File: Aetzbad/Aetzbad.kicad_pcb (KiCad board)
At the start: 2 copper layers, 13 parts, among them J1 CONN_01X04_MALE, J2 CONN_01X04_MALE, J3 CONN_01X04_MALE, J4 CONN_01X03_MALE, J5 CONN_01X03, Q1 BC547

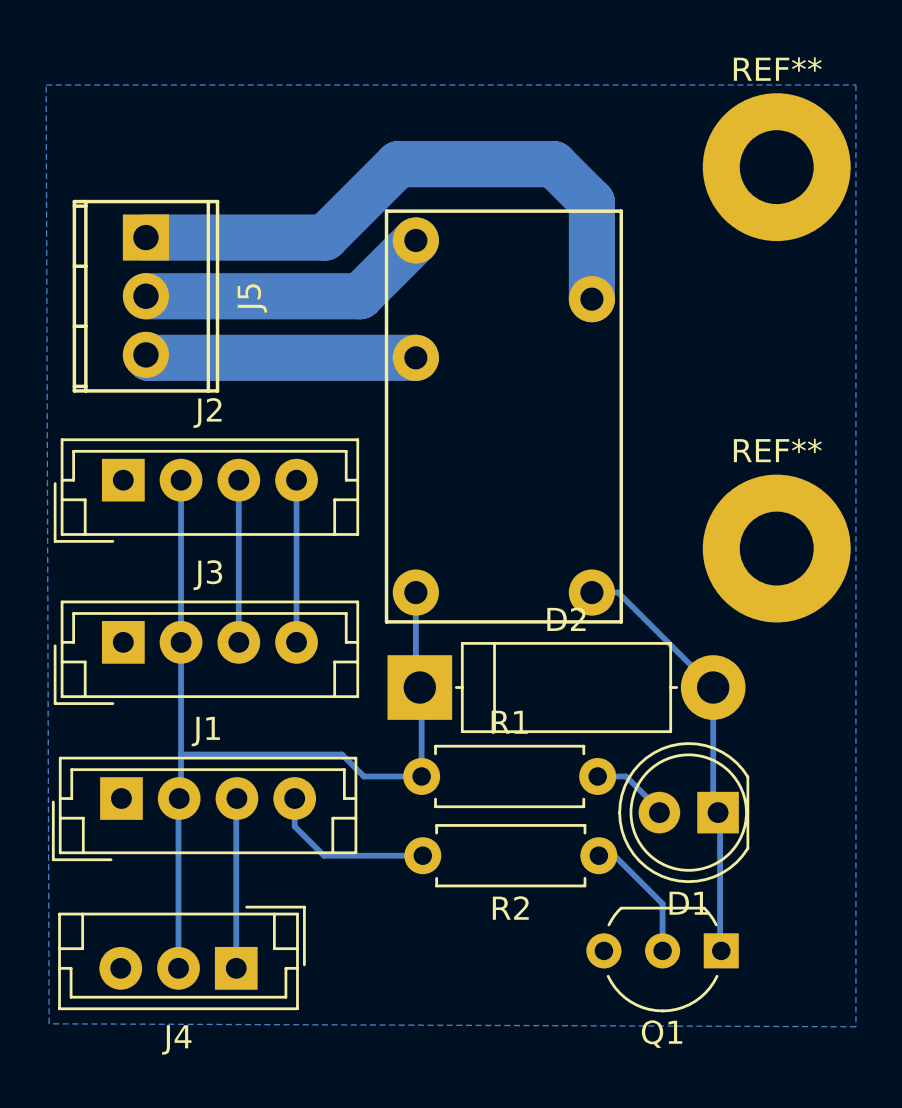
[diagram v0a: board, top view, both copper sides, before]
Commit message: added 3d Relais
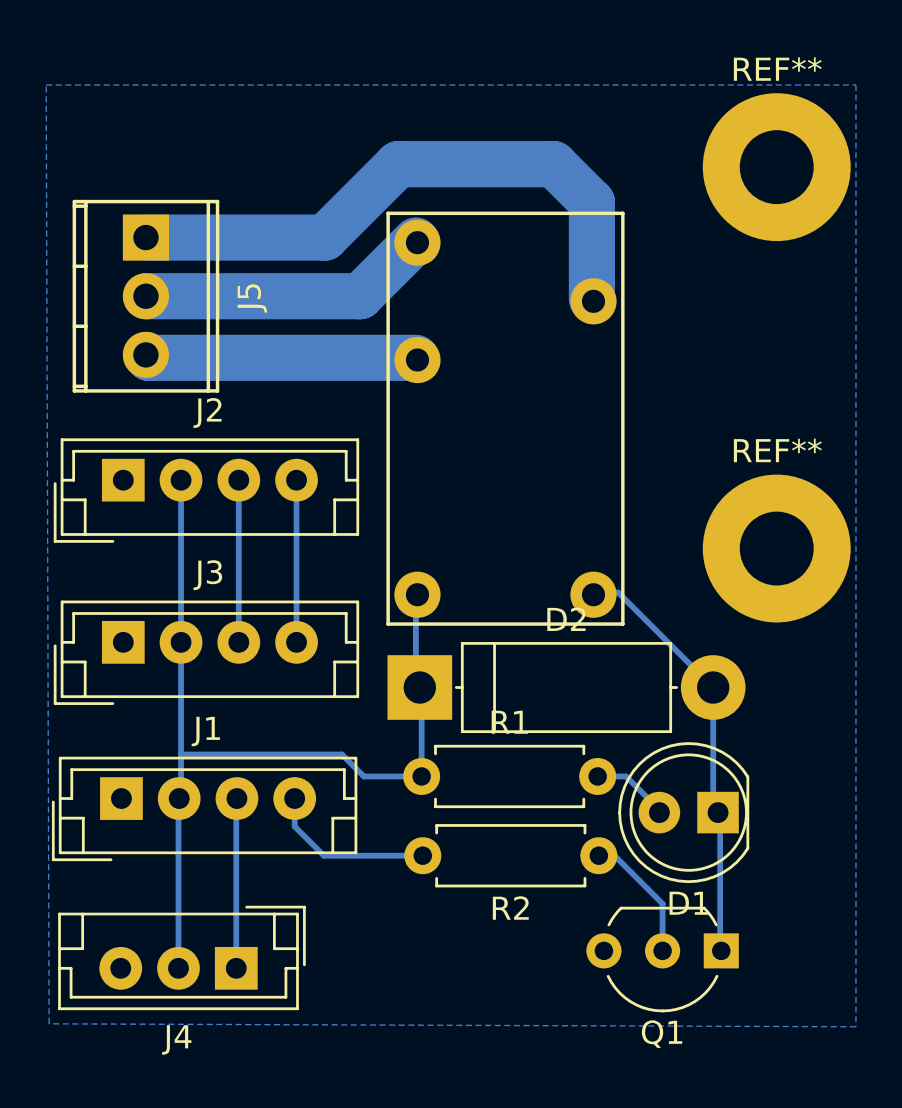
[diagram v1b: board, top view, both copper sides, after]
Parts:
- moved RL1 1.67 mm to (183.1, 102.1), turned to 270 degrees
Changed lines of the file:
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@@
-(kicad_pcb (version 4) (host pcbnew 4.0.6)
+(kicad_pcb (version 4) (host pcbnew 4.0.7)
   (general
     (links 22)
     (no_connects 0)
-    (area 0 0 0 0)
+    (area 161.523571 86.519 206.033858 130.45)
     (thickness 1.6)
     (drawings 6)
@@
     (add_net "Net-(J5-Pad3)")
   )
-  (module relay:JZC-11F (layer F.Cu)
-    (at 182.88 103.759)
-    (fp_text reference RL1 (at 0 0.5) (layer F.SilkS) hide
-      (effects (font (size 1 1) (thickness 0.15)))
-    )
-    (fp_text value JZC-11F (at 0 -11.43) (layer F.Fab)
-      (effects (font (size 1 1) (thickness 0.15)))
-    )
-    (fp_line (start -5.08 7.62) (end 5.08 7.62) (layer F.SilkS) (width 0.15))
-    (fp_line (start 5.08 7.62) (end 5.08 -10.16) (layer F.SilkS) (width 0.15))
-    (fp_line (start 5.08 -10.16) (end -5.08 -10.16) (layer F.SilkS) (width 0.15))
-    (fp_line (start -5.08 -10.16) (end -5.08 7.62) (layer F.SilkS) (width 0.15))
-    (pad 1 thru_hole circle (at -3.81 6.35) (size 2 2) (drill 1) (layers *.Cu *.Mask)
-      (net 3 VCC))
-    (pad 2 thru_hole circle (at 3.81 6.35) (size 2 2) (drill 1) (layers *.Cu *.Mask)
-      (net 1 "Net-(D1-Pad1)"))
-    (pad 3 thru_hole circle (at 3.81 -6.35) (size 2 2) (drill 1) (layers *.Cu *.Mask)
-      (net 10 "Net-(J5-Pad1)"))
-    (pad 4 thru_hole circle (at -3.81 -3.81) (size 2 2) (drill 1) (layers *.Cu *.Mask)
-      (net 9 "Net-(J5-Pad3)"))
-    (pad 5 thru_hole circle (at -3.81 -8.89) (size 2 2) (drill 1) (layers *.Cu *.Mask)
-      (net 11 "Net-(J5-Pad2)"))
-  )
   (module LEDs:LED_D5.0mm (layer F.Cu)
     (at 192.151 119.634 180)
@@
     (pad 1 thru_hole circle (at 0 0) (size 6.4 6.4) (drill 3.2) (layers *.Cu *.Mask))
   )
+  (module relay:JZC-11F (layer F.Cu)
+    (at 183.134 102.108 270)
+    (fp_text reference RL1 (at 2.245 0.185 360) (layer F.SilkS) hide
+      (effects (font (size 1 1) (thickness 0.15)))
+    )
+    (fp_text value JZC-11F (at -9.685 0.185 360) (layer F.Fab)
+      (effects (font (size 1 1) (thickness 0.15)))
+    )
+    (fp_line (start 9.365 5.265) (end 9.365 -4.895) (layer F.SilkS) (width 0.15))
+    (fp_line (start 9.365 -4.895) (end -8.415 -4.895) (layer F.SilkS) (width 0.15))
+    (fp_line (start -8.415 -4.895) (end -8.415 5.265) (layer F.SilkS) (width 0.15))
+    (fp_line (start -8.415 5.265) (end 9.365 5.265) (layer F.SilkS) (width 0.15))
+    (pad 1 thru_hole circle (at 8.095 3.995) (size 2 2) (drill 1) (layers *.Cu *.Mask)
+      (net 3 VCC))
+    (pad 2 thru_hole circle (at 8.095 -3.625) (size 2 2) (drill 1) (layers *.Cu *.Mask)
+      (net 1 "Net-(D1-Pad1)"))
+    (pad 3 thru_hole circle (at -4.605 -3.625) (size 2 2) (drill 1) (layers *.Cu *.Mask)
+      (net 10 "Net-(J5-Pad1)"))
+    (pad 4 thru_hole circle (at -2.065 3.995) (size 2 2) (drill 1) (layers *.Cu *.Mask)
+      (net 9 "Net-(J5-Pad3)"))
+    (pad 5 thru_hole circle (at -7.145 3.995) (size 2 2) (drill 1) (layers *.Cu *.Mask)
+      (net 11 "Net-(J5-Pad2)"))
+    (model ../../../../../../Users/Service/Desktop/Belichter/Aetzbad/jzc-11f.wrl
+      (at (xyz 0.019685 0 0))
+      (scale (xyz 0.393701 0.393701 0.393701))
+      (rotate (xyz 0 0 0))
+    )
+  )
   (gr_line (start 198.32 128.33) (end 198.37 128.33) (angle 90) (layer Margin) (width 0.2))
   (gr_line (start 198.32 129.04) (end 198.32 128.33) (angle 90) (layer Margin) (width 0.2))
@@
   (gr_line (start 198.34 88.01) (end 163 88.01) (angle 90) (layer Margin) (width 0.2))
   (gr_line (start 198.34 128.73) (end 198.34 88.01) (angle 90) (layer Margin) (width 0.2))
-  (segment (start 186.69 110.109) (end 187.829 110.109) (width 0.25) (layer B.Cu) (net 1))
   (segment (start 187.829 110.109) (end 191.94 114.22) (width 0.25) (layer B.Cu) (net 1))
   (segment (start 192.24 125.57) (end 192.29 125.62) (width 0.25) (layer B.Cu) (net 1))
@@
   (segment (start 192.24 119.6) (end 192.24 125.57) (width 0.25) (layer B.Cu) (net 1))
   (segment (start 191.94 119.3) (end 192.24 119.6) (width 0.25) (layer B.Cu) (net 1))
+  (segment (start 186.69 110.109) (end 187.829 110.109) (width 0.25) (layer B.Cu) (net 1))
   (segment (start 188.17 118.07) (end 189.7 119.6) (width 0.25) (layer B.Cu) (net 2))
   (segment (start 186.94 118.07) (end 188.17 118.07) (width 0.25) (layer B.Cu) (net 2))
@@
   (segment (start 178.308 91.567) (end 185.039 91.567) (width 2) (layer B.Cu) (net 10))
   (segment (start 175.133 94.742) (end 178.308 91.567) (width 2) (layer B.Cu) (net 10))
+  (segment (start 176.657 97.282) (end 179.07 94.869) (width 2) (layer B.Cu) (net 11))
   (segment (start 167.386 97.282) (end 176.657 97.282) (width 2) (layer B.Cu) (net 11))
-  (segment (start 176.657 97.282) (end 179.07 94.869) (width 2) (layer B.Cu) (net 11))
   (segment (start 186.99 121.5) (end 187.667 121.5) (width 0.25) (layer B.Cu) (net 12))
   (segment (start 187.667 121.5) (end 189.75 123.583) (width 0.25) (layer B.Cu) (net 12))
